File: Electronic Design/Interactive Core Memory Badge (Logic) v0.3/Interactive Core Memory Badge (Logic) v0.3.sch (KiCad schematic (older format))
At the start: 59 parts, among them Q1 MMBT4403LT1G, Q10 MMBT4401LT1G, Q11 MMBT4403LT1G, Q12 MMBT4401LT1G, Q13 MMBT4403LT1G, Q14 MMBT4401LT1G, Q15 MMBT4403LT1G, Q16 MMBT4401LT1G, Q17 MMBT4403LT1G, Q18 MMBT4401LT1G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

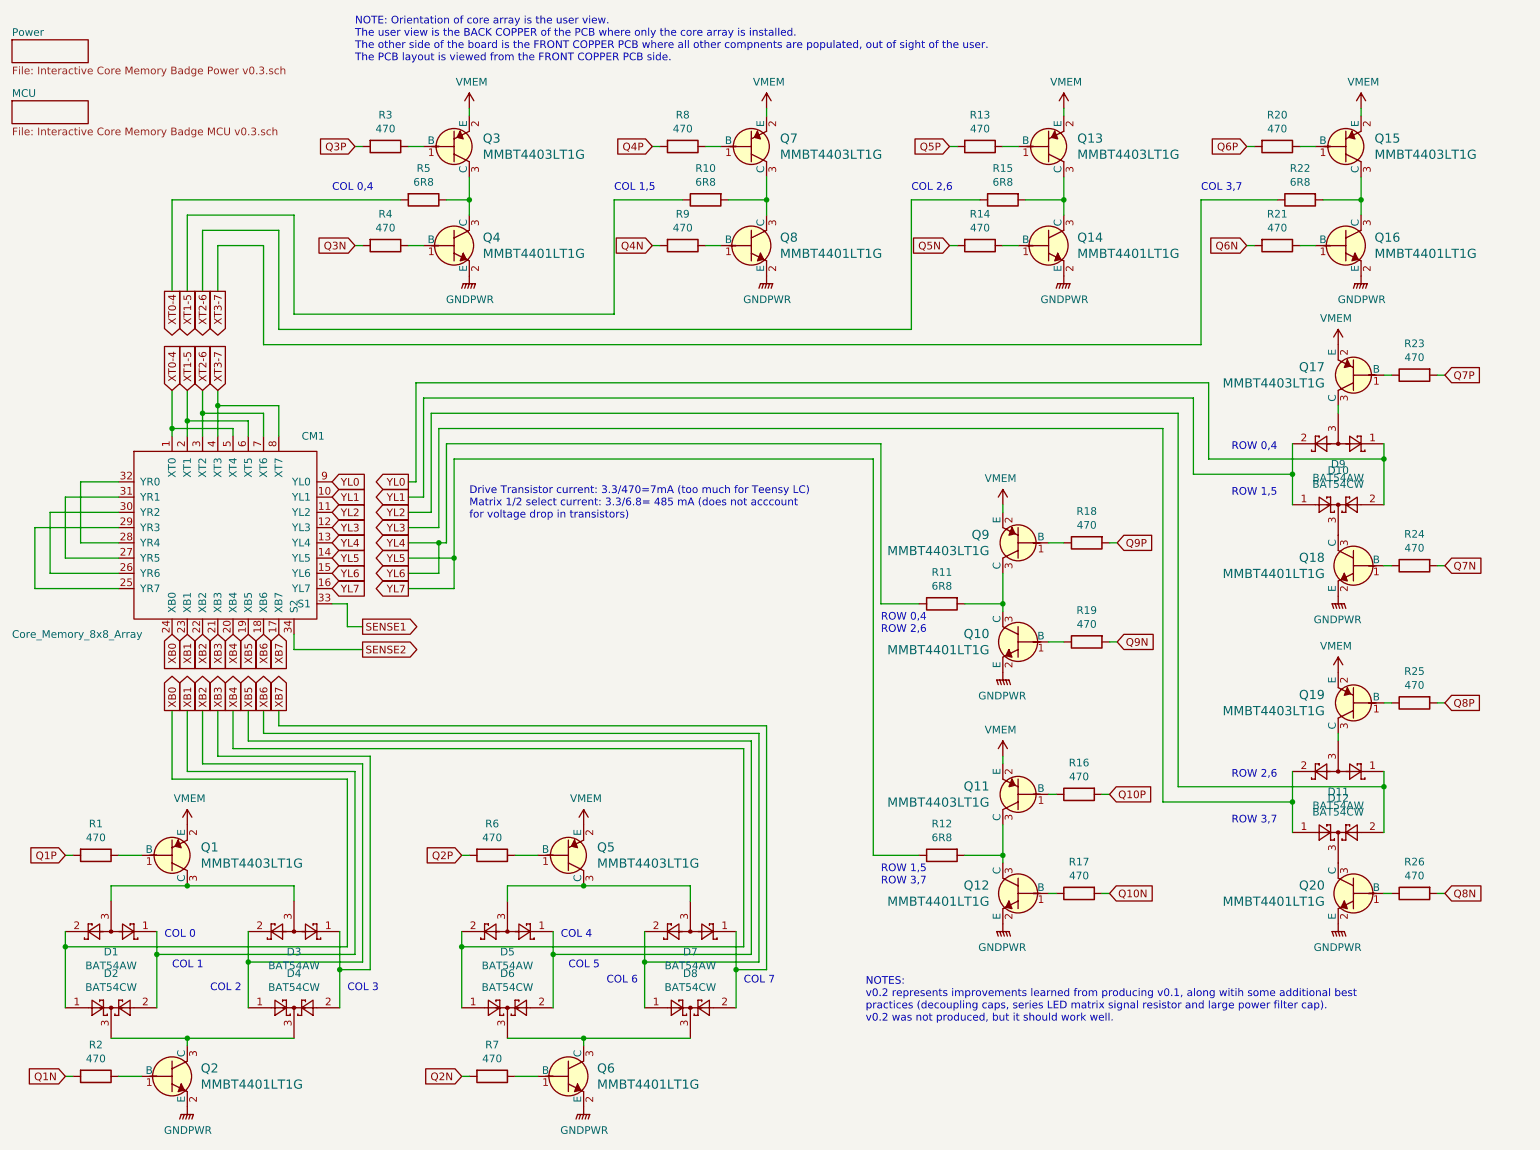
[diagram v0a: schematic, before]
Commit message: Split V0.3 into two project boards
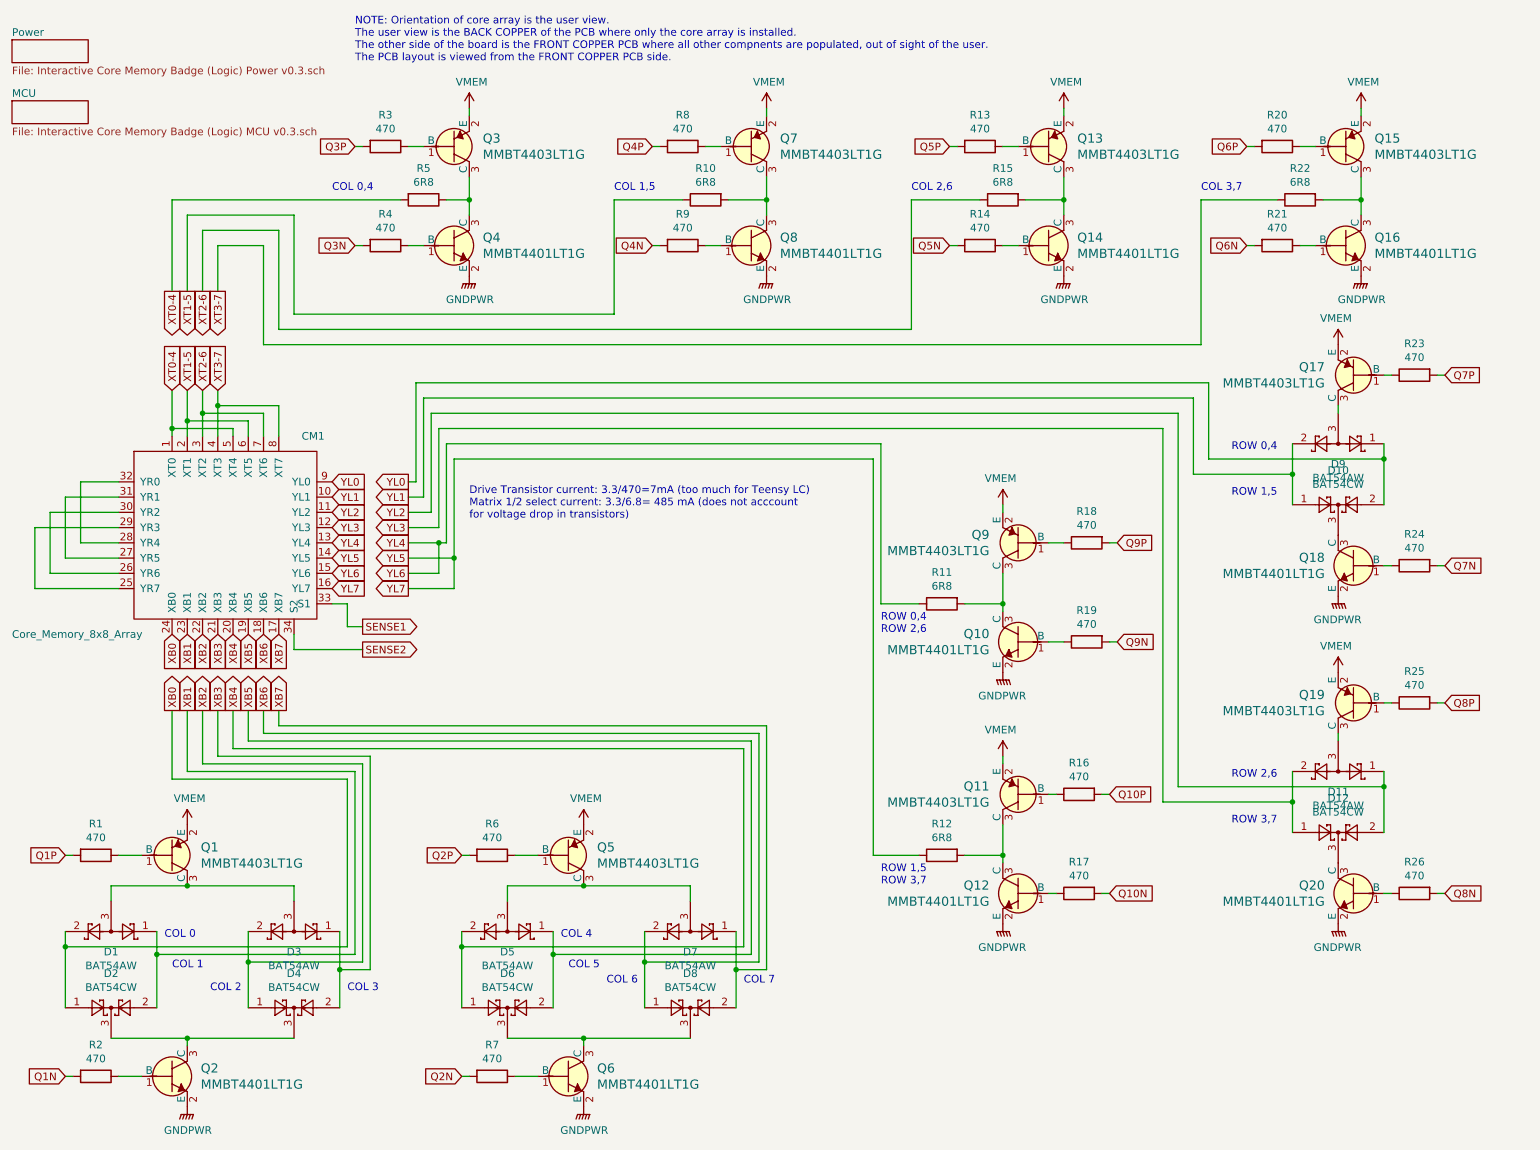
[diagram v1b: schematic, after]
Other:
- note removed: "NOTES:\nv0.2 represents improvements learned from producing v0.1, along witih some additional best\npractices (decoupling caps, series LED matrix signal resistor and large power filter cap).\nv0.2 was not produced, but it should work well."
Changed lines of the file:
@@
 EESchema Schematic File Version 4
-LIBS:Interactive Core Memory Badge v0.3-cache
+LIBS:Interactive Core Memory Badge (Logic) v0.3-cache
 EELAYER 29 0
 EELAYER END
@@
 encoding utf-8
 Sheet 1 3
-Title "Core 64 - Interactive Core Memory Badge (Dual Board)"
+Title "Core 64 - Interactive Core Memory Badge (Logic)"
 Date "2020-03-15"
 Rev "0.3"
@@
 U 5D254AE8
 F0 "Power" 50
-F1 "Interactive Core Memory Badge Power v0.3.sch" 50
+F1 "Interactive Core Memory Badge (Logic) Power v0.3.sch" 50
 $EndSheet
 $Sheet
@@
 U 5D2551FF
 F0 "MCU" 50
-F1 "Interactive Core Memory Badge MCU v0.3.sch" 50
+F1 "Interactive Core Memory Badge (Logic) MCU v0.3.sch" 50
 $EndSheet
 Text GLabel 1750 4600 3    50   Input ~ 0
@@
 	1    0    0    -1
 $EndComp
-Text Notes 6300 7150 0    50   ~ 0
-NOTES:\nv0.2 represents improvements learned from producing v0.1, along witih some additional best\npractices (decoupling caps, series LED matrix signal resistor and large power filter cap).\nv0.2 was not produced, but it should work well.
 Text Notes 3700 3850 0    50   ~ 0
 Drive Transistor current: 3.3/470=7mA (too much for Teensy LC)\nMatrix 1/2 select current: 3.3/6.8= 485 mA (does not acccount \nfor voltage drop in transistors)
